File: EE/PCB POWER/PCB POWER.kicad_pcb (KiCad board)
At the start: 2 copper layers, 84 x 84 mm, 48 parts, among them IC1 DRV8220DRLR, J14 B2B-PH-K-S, J15 B2B-PH-K-S, J16 B2B-PH-K-S, J17 B5B-PH-K-S, J2 1752104, J3 1752104, J5 B2B-PH-K-S, Q1 IPD30N08S2L21ATMA1, Q2 IPD30N08S2L21ATMA1, U1 MIC4427YM-TR, U2 742792510, U3 RPM5.0-6.0, U4 7427932

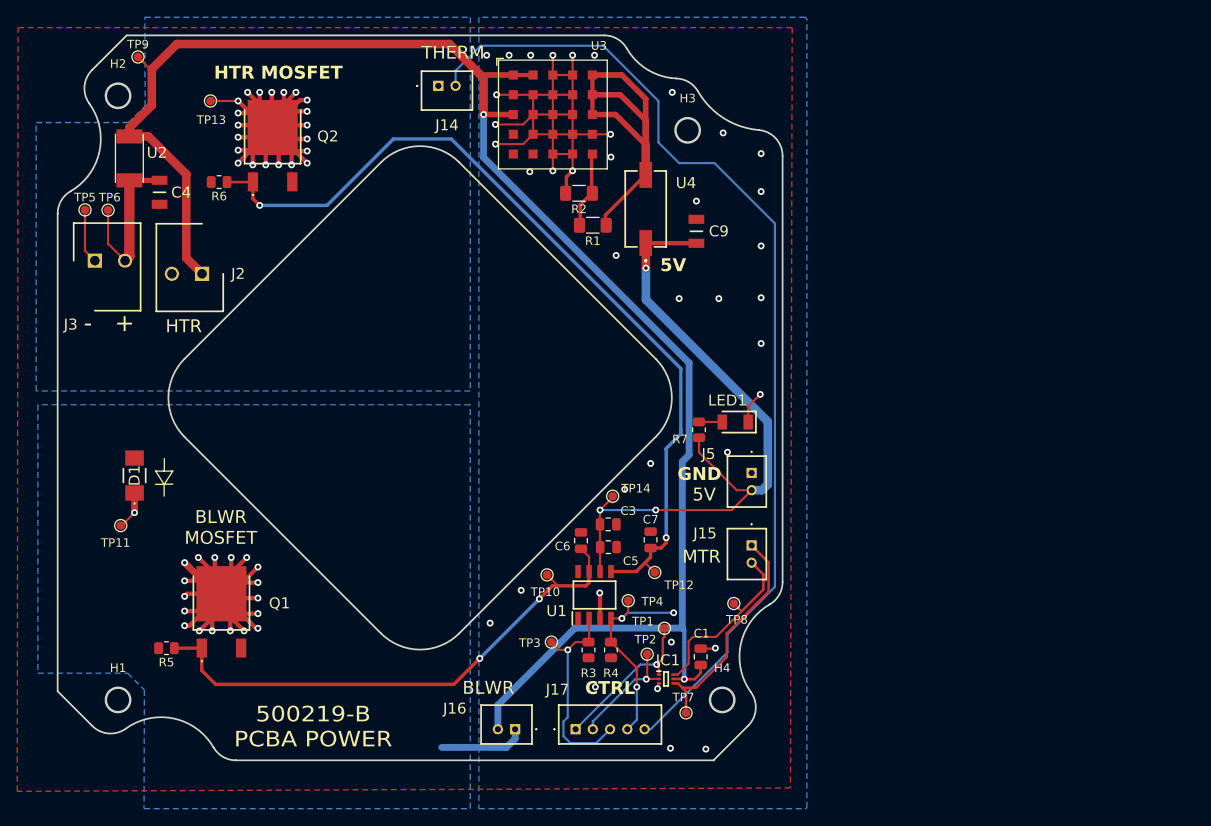
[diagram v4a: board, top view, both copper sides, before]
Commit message: Widened traces
Widened traces further.  Added more text to front silkscreen layer.
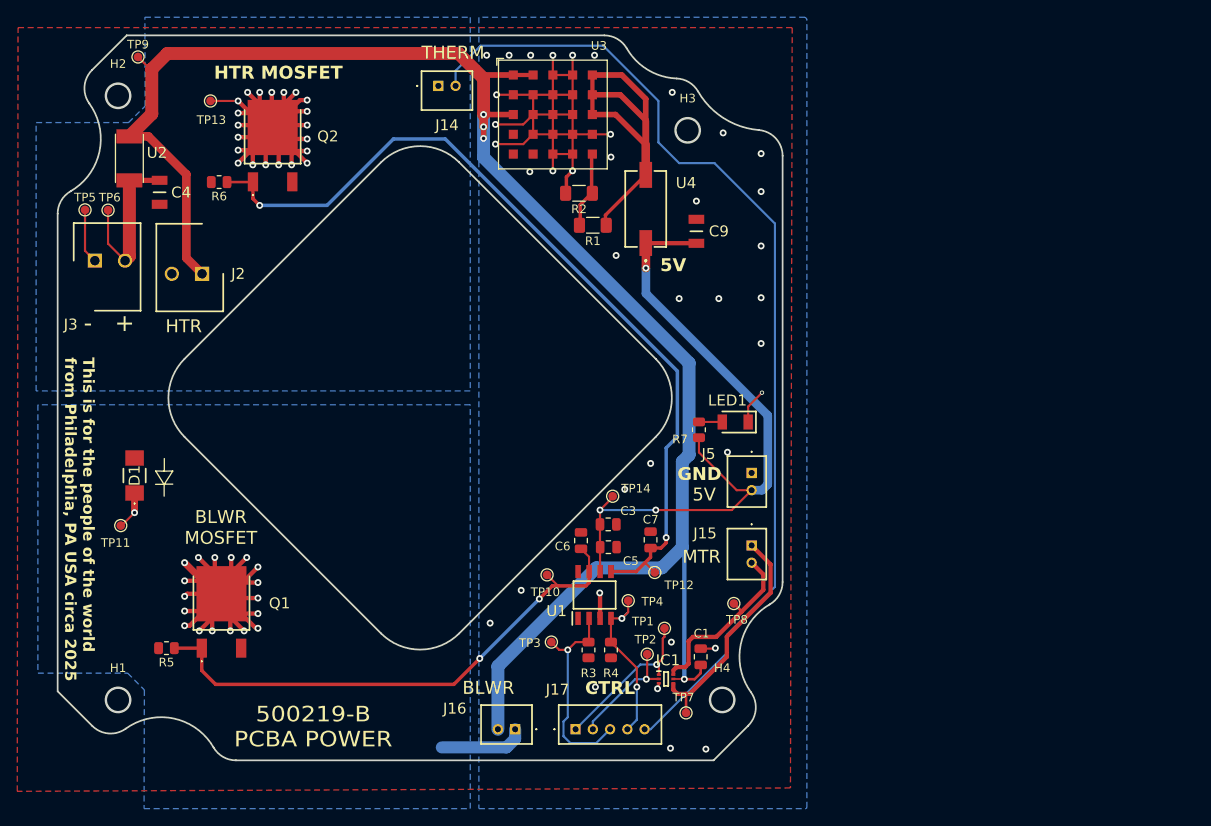
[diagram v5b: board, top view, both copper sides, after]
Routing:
- net Net-(IC1-VM): track 194.8 -> 203.7 mm, vias 2 -> 4
- net HTR_PID: track 24.9 -> 19.3 mm, vias 3 -> 2
- net Net-(U1-OUTB): track 100.0 -> 99.2 mm
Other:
- board text added: "This is for the people of the world from Philadelphia, PA USA circa 2025"

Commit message: Cleaned up libraries and rearranged files
For folder "EE":
Created a symbol library "DaisyBio_mira" that contains the only 2 parts that weren't available stock (U1 and U4, formerly IC1) from PCB POWER

For PCB POWER:
Changed "IC1" to "U4"
Changed the ferrite bead to "FB1"
Changed all the custom symbols to generic stock ones, such as: all the connectors, NMOS's, capacitors, inductor, ferrite bead, LEDs, diodes
Changed symbol "R" to "R_US".
Copied all the footprints that were in random small one-part libraries into "DaisyBio_mira"
Moved all the gerbers into dated folders into another folder "Outputs"
Moved all the now-deprecated small libraries into "Downloaded Assets"
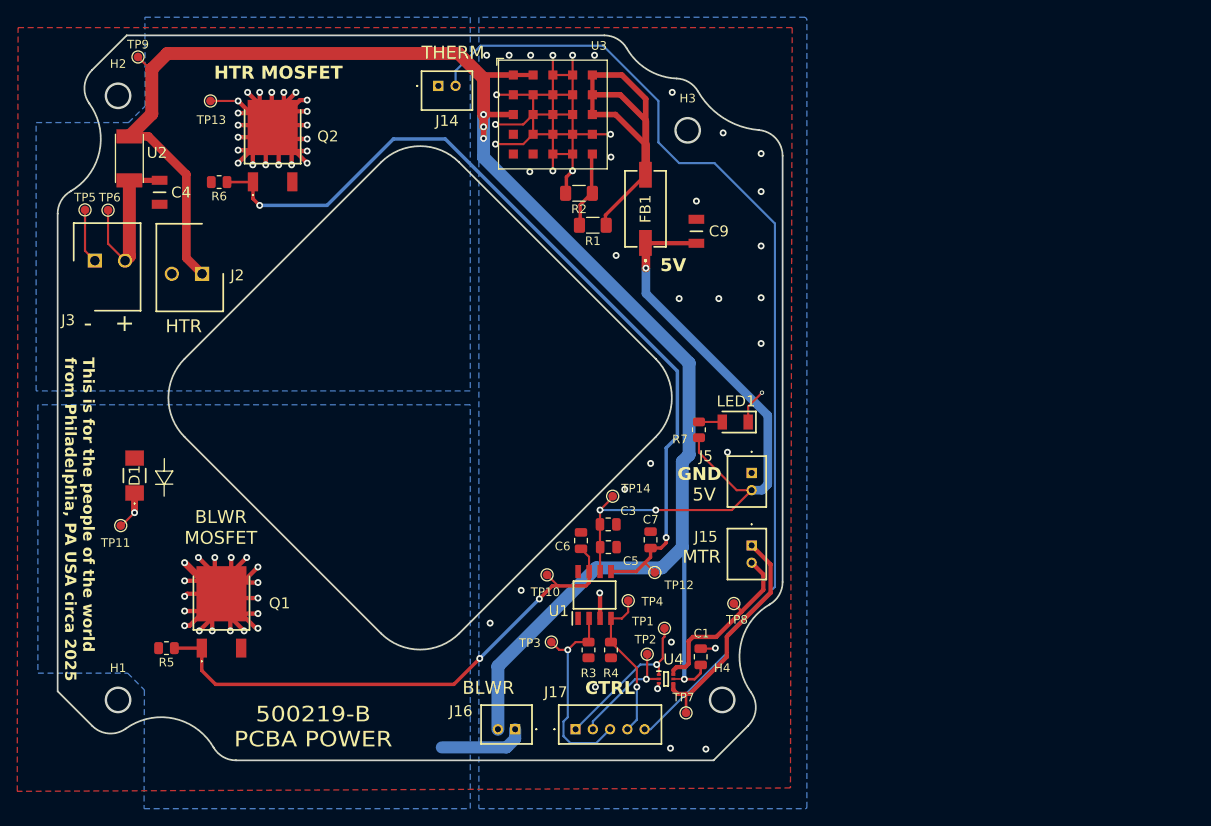
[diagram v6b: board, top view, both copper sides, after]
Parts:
- removed IC1: DRV8220DRLR, DaisyBio_Mira:SOTFL50P160X60-6N
- added FB1: 7427932, DaisyBio_Mira:7427932, F.Cu at (126.1, 78.1)
- J14, J15, J16, J5: footprint B2B-PH-K-S:B2BPHKS -> DaisyBio_Mira:B2BPHKS
- J17: footprint B5B-PH-K-S:B5BPHKS -> DaisyBio_Mira:B5BPHKS
- J2, J3: footprint 1752104:SHDR2W90P0X350_1X2_760X1000X1255P -> DaisyBio_Mira:SHDR2W90P0X350_1X2_760X1000X1255P
- LED1: footprint 150120VS75000:LEDC3216X78N -> DaisyBio_Mira:LEDC3216X78N
- U4: value 7427932 -> DRV8220DRLR; footprint DaisyBio_Mira:7427932 -> DaisyBio_Mira:SOTFL50P160X60-6N
- moved U4 54.5 mm to (128.5, 132.6), turned to 0 degrees
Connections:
- C1 pad 2: Net-(IC1-VM) -> Net-(J16-Pin_2)
- C3 pad 1: Net-(U1-VS) -> Net-(J5-Pin_2)
- C5 pad 1: Net-(U1-VS) -> Net-(J5-Pin_2)
- C9 pad 2: Net-(U1-VS) -> Net-(J5-Pin_2)
- J16 pad 2: Net-(IC1-VM) -> Net-(J16-Pin_2)
- J2 pad 1: Net-(IC1-VM) -> Net-(J16-Pin_2)
- J5 pad 2: Net-(U1-VS) -> Net-(J5-Pin_2)
- R7 pad 1: Net-(U1-VS) -> Net-(J5-Pin_2)
- TP14 pad 1: Net-(U1-VS) -> Net-(J5-Pin_2)
- TP9 pad 1: Net-(IC1-VM) -> Net-(J16-Pin_2)
- U1 pad 6: Net-(U1-VS) -> Net-(J5-Pin_2)
- U2 pad 2: Net-(IC1-VM) -> Net-(J16-Pin_2)
- U3 pad A1: Net-(IC1-VM) -> Net-(J16-Pin_2)
- U3 pad A2: Net-(IC1-VM) -> Net-(J16-Pin_2)
- U3 pad C1: Net-(IC1-VM) -> Net-(J16-Pin_2)
- U4 pad 1: Net-(U1-VS) -> MTR_PID1
- U4 pad 2: Net-(U3-Sense) -> MTR_PID2
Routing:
- net Net-(J16-Pin_2): track 0.00 -> 203.7 mm, vias 0 -> 4
- net Net-(IC1-VM): track 203.7 -> 0.00 mm, vias 4 -> 0
- net Net-(U1-VS): track 79.3 -> 0.00 mm, vias 3 -> 0
- net Net-(J5-Pin_2): track 0.00 -> 79.3 mm, vias 0 -> 3
- net HTR_PID: track 19.3 -> 18.4 mm, vias 2 -> 1
